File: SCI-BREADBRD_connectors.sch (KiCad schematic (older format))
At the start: 0 parts

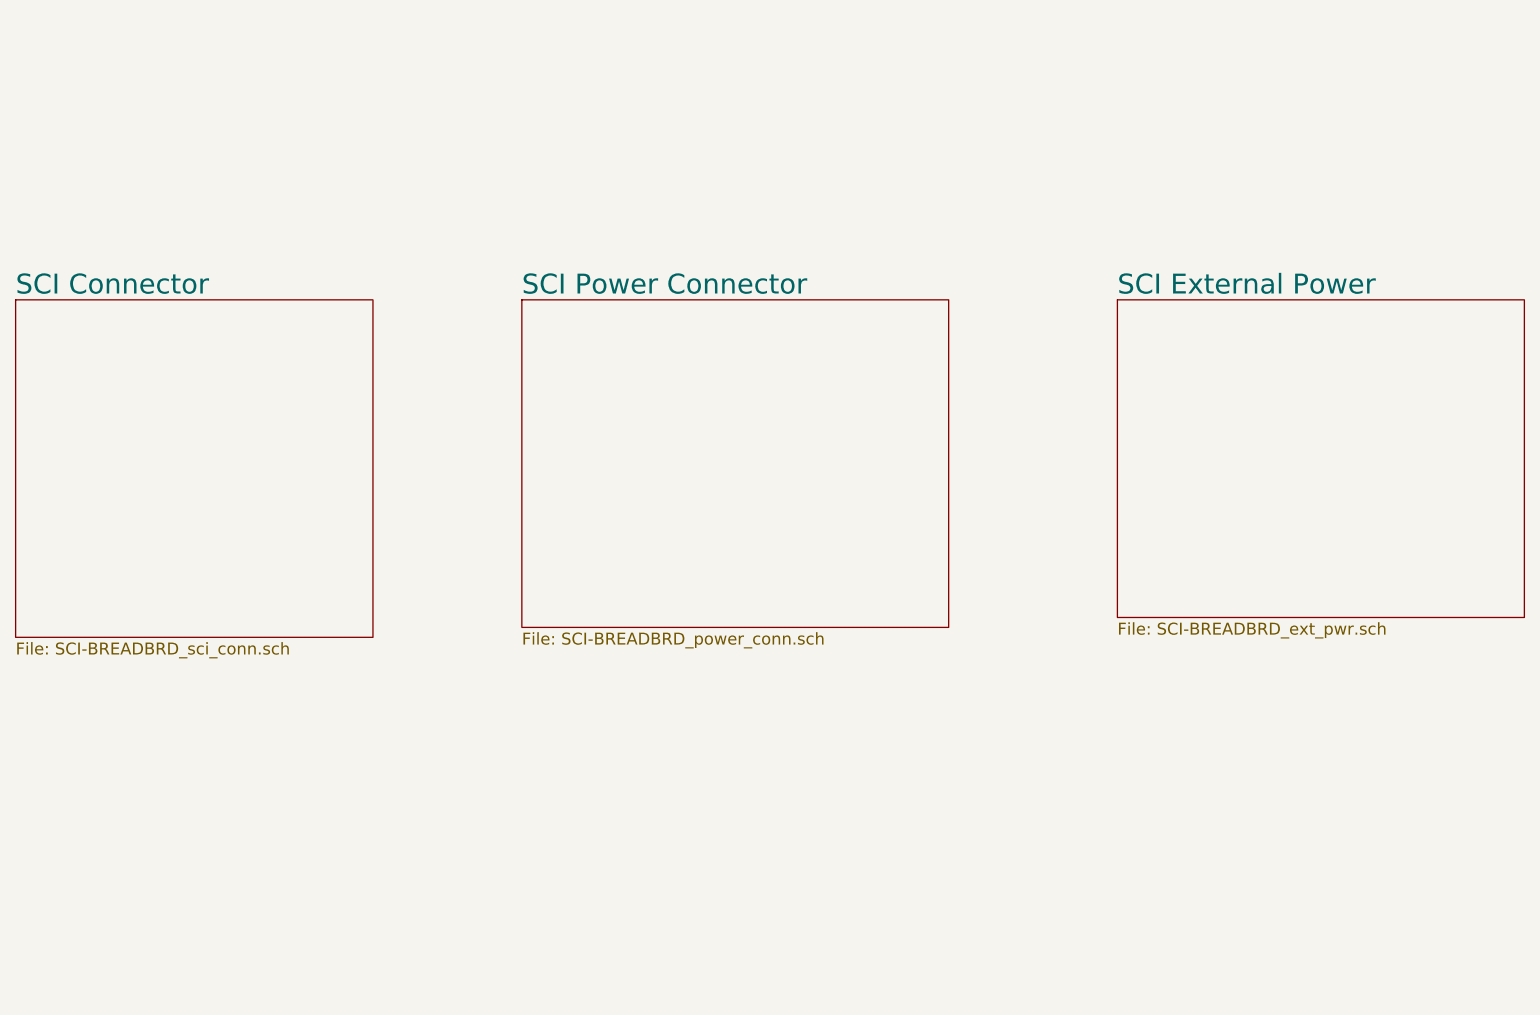
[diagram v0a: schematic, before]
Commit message: Completed ERC. Added some power flags and fixed mis-connected pins.
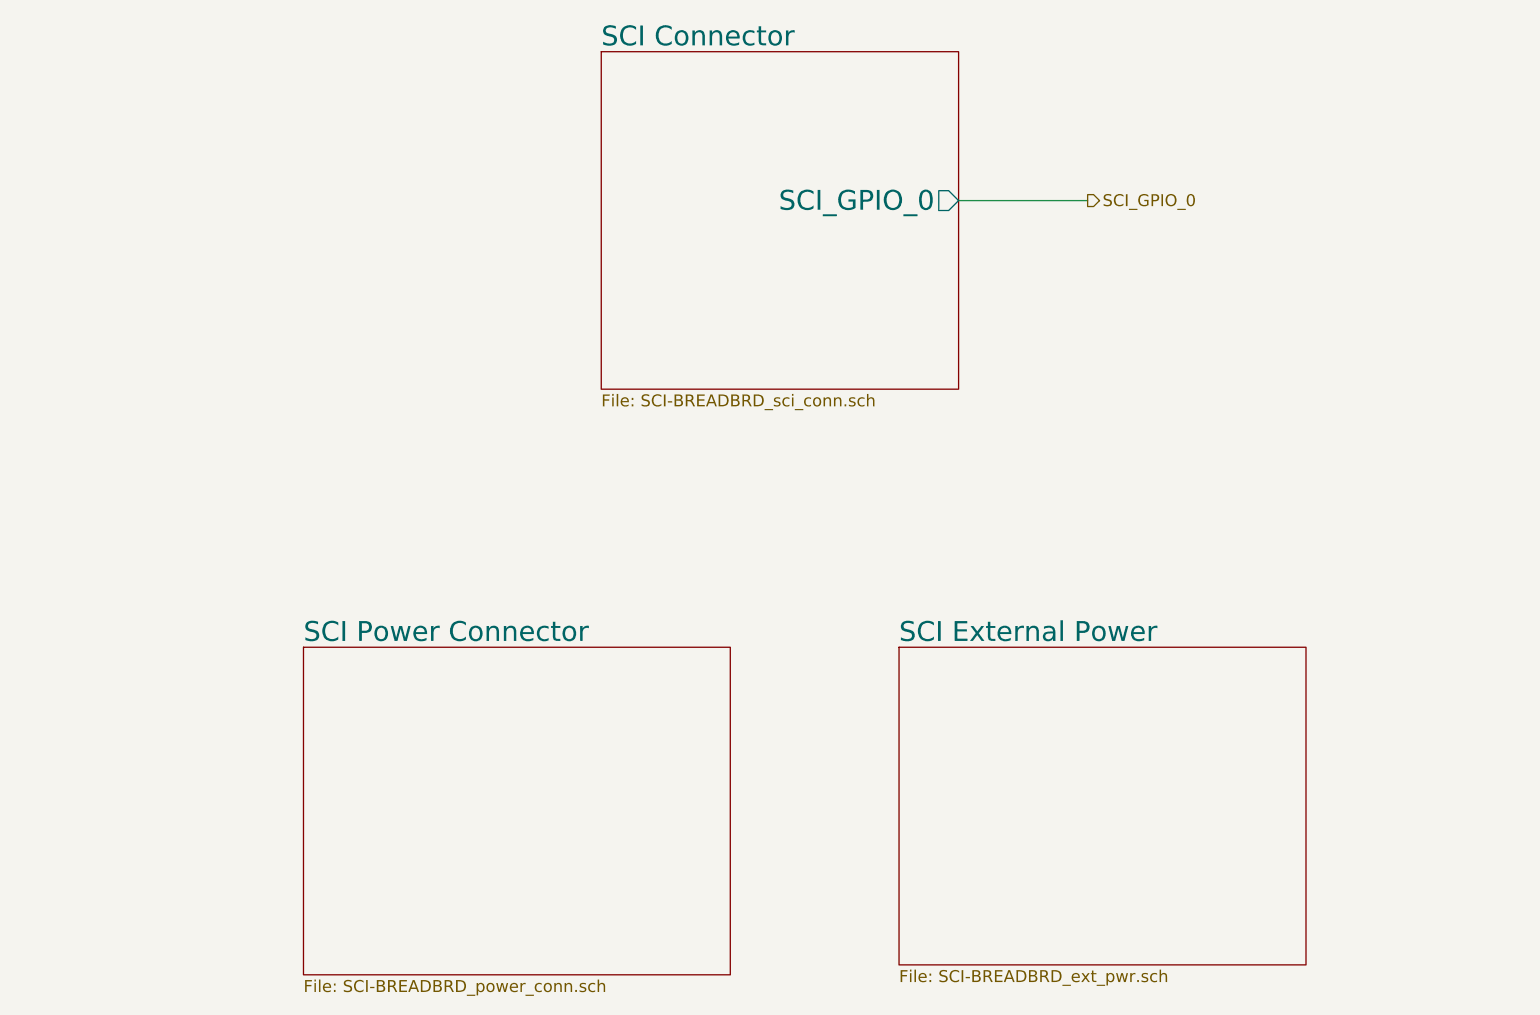
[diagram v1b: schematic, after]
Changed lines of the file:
@@
-EESchema Schematic File Version 2  date Fri 27 Apr 2012 09:11:54 AM EDT
+EESchema Schematic File Version 2  date Fri 27 Apr 2012 11:11:24 AM EDT
 LIBS:custom_transistors
 LIBS:TI_custom
@@
 $EndDescr
 $Sheet
-S 4200 3100 2150 1650
+S 3100 4850 2150 1650
 U 4F9A6177
 F0 "SCI Power Connector" 100
@@
 $EndSheet
 $Sheet
-S 7200 3100 2050 1600
+S 6100 4850 2050 1600
 U 4F9A6281
 F0 "SCI External Power" 100
@@
 $EndSheet
 $Sheet
-S 1650 3100 1800 1700
+S 4600 1850 1800 1700
 U 4F9A63AC
 F0 "SCI Connector" 100
 F1 "SCI-BREADBRD_sci_conn.sch" 60
+F2 "SCI_GPIO_0" O R 6400 2600 100
 $EndSheet
+Text HLabel 7050 2600 2    60   Output ~ 0
+SCI_GPIO_0
+Wire Wire Line
+	6400 2600 7050 2600
 $EndSCHEMATC
